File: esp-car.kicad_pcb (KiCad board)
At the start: 2 copper layers, 29 parts, among them J1 Conn_01x07_Socket, J2 Conn_01x07_Socket, U1 ESP32-DEVKIT-V1, U3 L293D

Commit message: esp_car 3.1
30/09 1:06
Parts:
- added ALI1: Conn_01x02_Socket, Connector_PinSocket_2.54mm:PinSocket_1x02_P2.54mm_Vertical, F.Cu at (180.9, 173.1)
- added INF_C1: Conn_01x06_Socket, Connector_PinSocket_2.54mm:PinSocket_1x06_P2.54mm_Vertical, F.Cu at (150.6, 53.0)
- added INF_FD1: Conn_01x06_Socket, Connector_PinSocket_2.54mm:PinSocket_1x06_P2.54mm_Vertical, F.Cu at (180.6, 49.4)
- added INF_FE1: Conn_01x06_Socket, Connector_PinSocket_2.54mm:PinSocket_1x06_P2.54mm_Vertical, F.Cu at (132.6, 49.4)
- added INF_TE1: Conn_01x06_Socket, Connector_PinSocket_2.54mm:PinSocket_1x06_P2.54mm_Vertical, F.Cu at (194.7, 155.8)
- added MotorD1: Conn_01x02_Socket, Connector_PinSocket_2.54mm:PinSocket_1x02_P2.54mm_Vertical, F.Cu at (185.5, 173.1)
- added MotorE1: Conn_01x02_Socket, Connector_PinSocket_2.54mm:PinSocket_1x02_P2.54mm_Vertical, F.Cu at (190.1, 173.1)
- J1, J2: moved to B.Cu
- moved EN2 87.1 mm to (178.2, 146.5)
- moved BotaoRotatorio1 76.2 mm to (138.0, 142.0)
- moved LED1 76.2 mm to (134.5, 194.1)
- moved R10 76.2 mm to (161.2, 158.0)
- moved Re2 76.2 mm to (166.2, 185.0)
- moved TelaOLED1 76.2 mm to (138.0, 156.5)
- moved BZ1 76.2 mm to (150.5, 168.8)
- moved C1 76.2 mm to (150.5, 183.5)
- moved EN1 76.2 mm to (143.0, 159.0)
- moved R220 76.2 mm to (161.2, 184.8)
- moved R9 76.2 mm to (161.2, 177.7)
- moved Re1 76.2 mm to (155.2, 154.5)
- moved U3 76.2 mm to (133.4, 168.9)
- moved giroscopio1 76.2 mm to (133.5, 148.9)
- moved R2 69.5 mm to (118.7, 46.8), turned to 180 degrees
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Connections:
- BotaoRotatorio1 pad 5: 5V -> 3.3V
- C1 pad 1: 5V -> GND
- C1 pad 2: 5VI -> VIN
- EN1 pad 1: Net-(EN1-Pin_1) -> OUTE
- EN1 pad 3: 5V -> 3.3V
- EN2 pad 1: Net-(EN2-Pin_1) -> OUTD
- EN2 pad 3: 5V -> 3.3V
- J1 pad 4: 5V -> 3.3V
- J2 pad 4: 5V -> 3.3V
- R1 pad 1: 5V -> 3.3V
- R2 pad 2: 5V -> 3.3V
- R3 pad 2: 5V -> 3.3V
- R4 pad 1: 5V -> 3.3V
- R5 pad 1: 5V -> 3.3V
- R6 pad 2: 5V -> 3.3V
- R7 pad 1: 5V -> 3.3V
- R8 pad 2: 5V -> 3.3V
- TelaOLED1 pad 4: 5V -> 3.3V
- U1 pad 1: unconnected-(U1-3V3-Pad1) -> 3.3V
- U1 pad 12: CD -> unconnected-(U1-RX0-Pad12)
- U1 pad 13: INF_C -> unconnected-(U1-TX0-Pad13)
- U1 pad 21: unconnected-(U1-D32-Pad21) -> CD
- U1 pad 30: 5V -> VIN
- U3 pad 1: 5V -> 3.3V
- U3 pad 16: 5V -> VIN
- U3 pad 9: 5V -> 3.3V
- giroscopio1 pad 7: 5V -> 3.3V

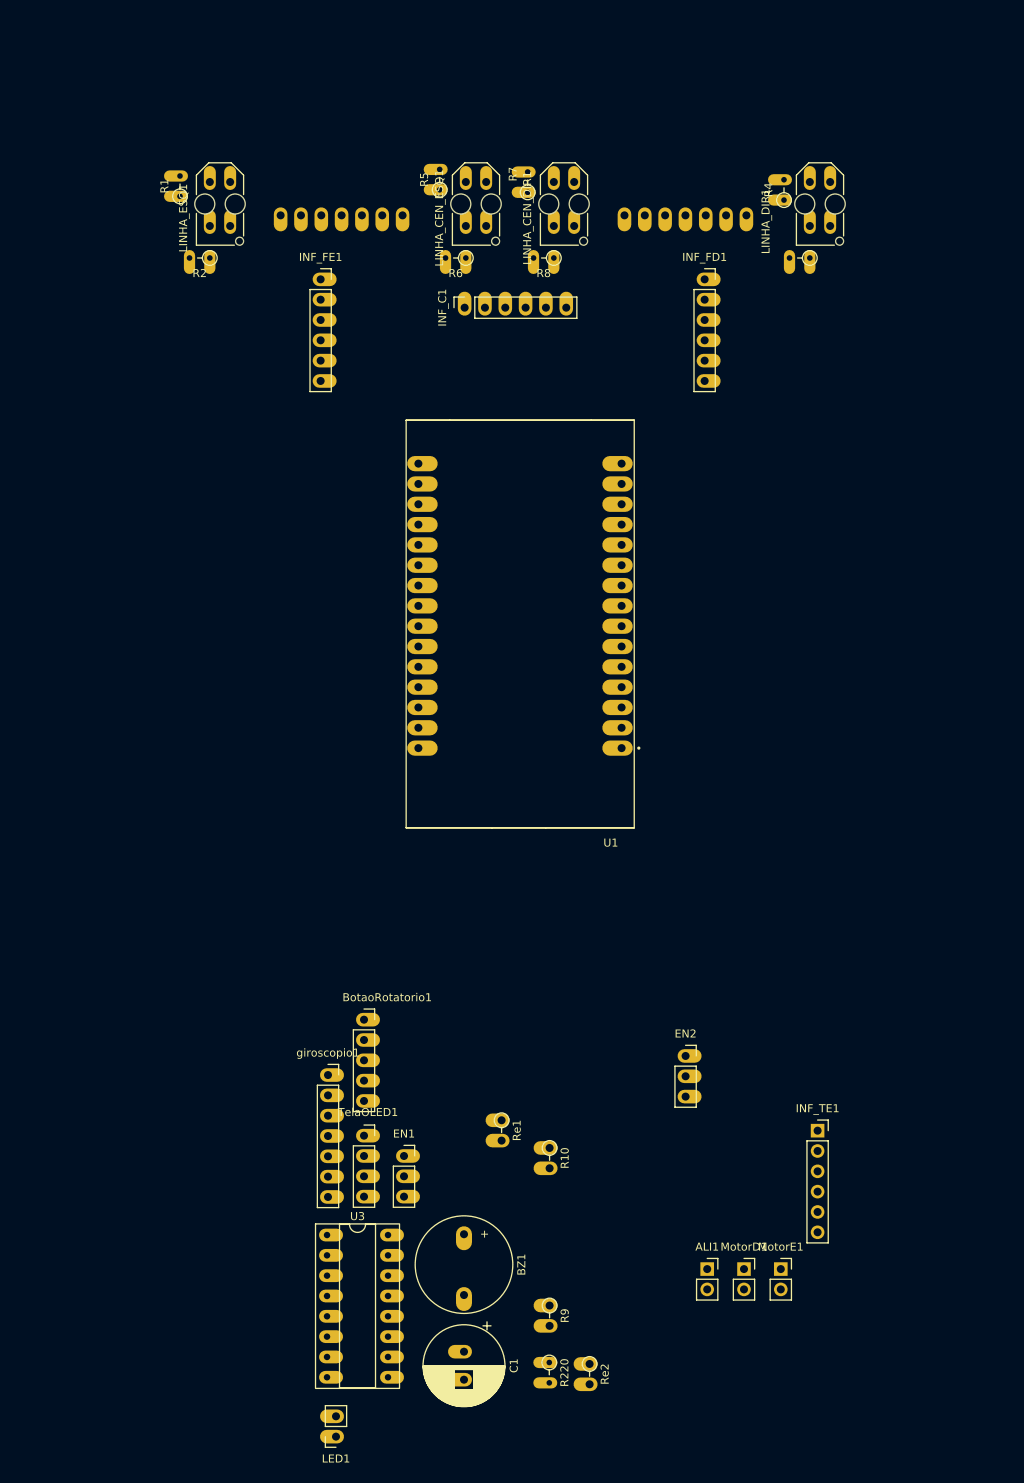
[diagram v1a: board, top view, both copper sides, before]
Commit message: esp-car 3.2
trilhas de cimas feitas, precisa arrumar resistores
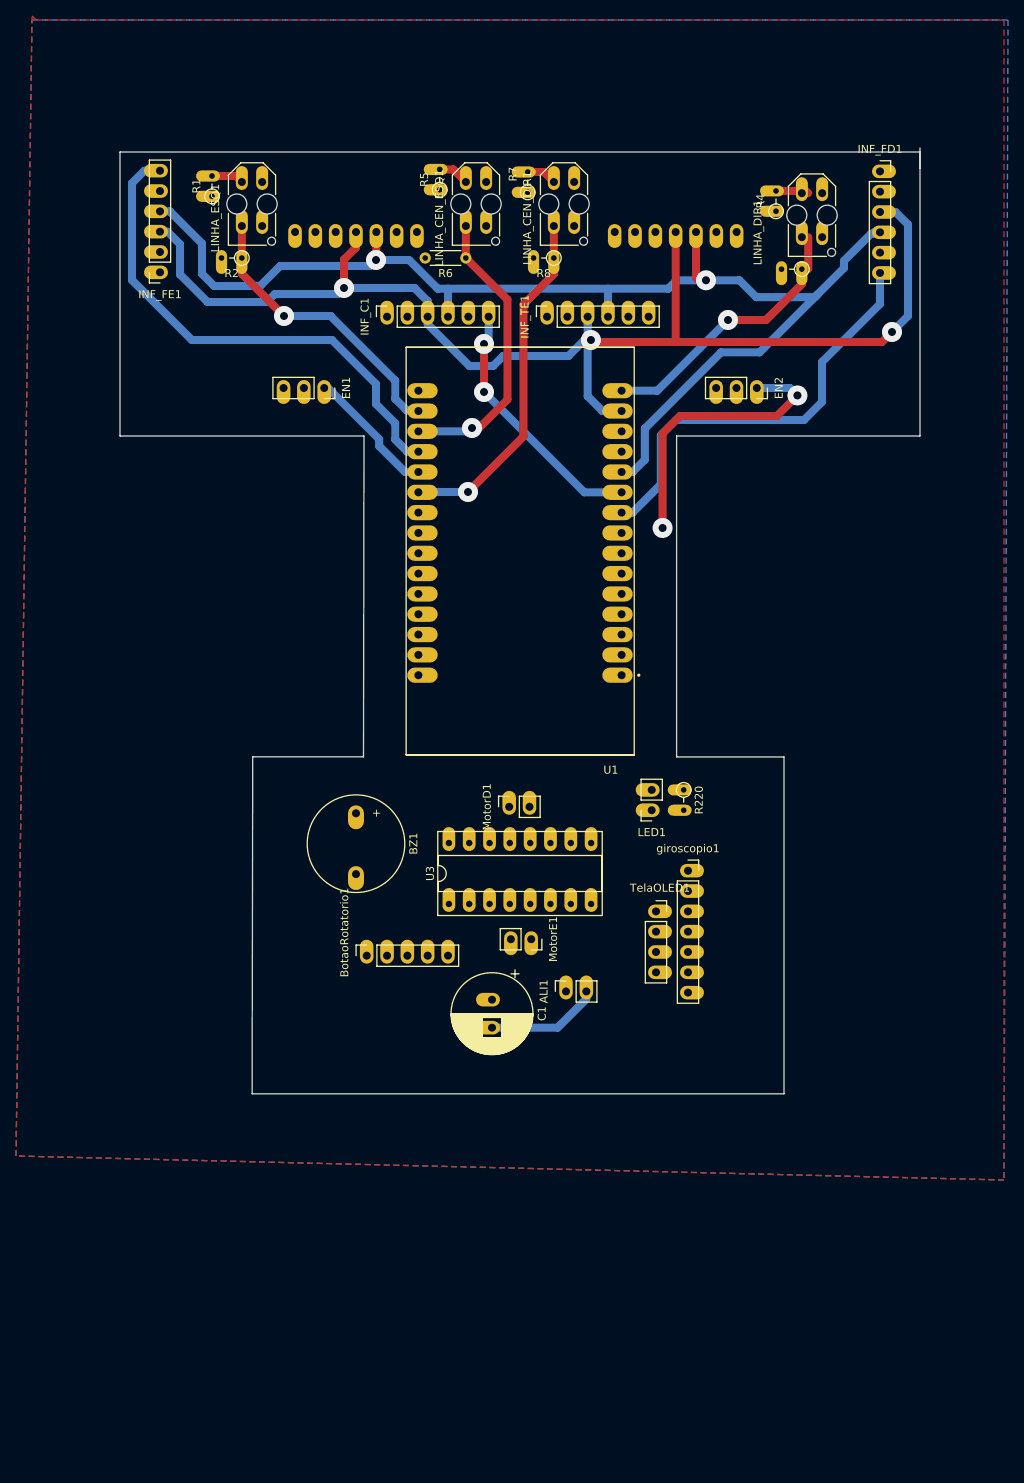
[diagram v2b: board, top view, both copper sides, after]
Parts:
- removed R10, R9: 1K, Resistor_THT:R_Axial_DIN0204_L3.6mm_D1.6mm_P2.54mm_Vertical
- removed Re1, Re2: 2K, Resistor_THT:R_Axial_DIN0204_L3.6mm_D1.6mm_P2.54mm_Vertical
- R6: footprint Resistor_THT:R_Axial_DIN0204_L3.6mm_D1.6mm_P2.54mm_Vertical -> Resistor_THT:R_Axial_DIN0204_L3.6mm_D1.6mm_P5.08mm_Horizontal
- moved INF_TE1 107.2 mm to (160.9, 54.1), turned to 90 degrees
- moved EN1 96.5 mm to (133.0, 63.0), turned to -90 degrees
- moved LED1 87.7 mm to (174.0, 115.8)
- moved EN2 84.0 mm to (187.1, 63.0), turned to -90 degrees
- moved R220 73.5 mm to (178.0, 113.2)
- moved MotorD1 64.8 mm to (156.2, 115.4), turned to 90 degrees
- moved BZ1 54.3 mm to (137.0, 116.2)
- moved giroscopio1 51.7 mm to (178.5, 123.3)
- moved MotorE1 51.7 mm to (158.9, 131.9), turned to -90 degrees
- moved TelaOLED1 46.0 mm to (174.5, 128.4)
- moved C1 44.1 mm to (154.0, 139.5)
- moved U3 44.1 mm to (148.6, 127.5), turned to 90 degrees
- moved ALI1 38.9 mm to (163.2, 138.4), turned to 90 degrees
- moved INF_FD1 25.7 mm to (202.5, 35.9)
- moved INF_FE1 20.1 mm to (112.5, 48.5), turned to 180 degrees
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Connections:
- J1 pad 2: SDA -> GND
- J1 pad 3: SCL -> 3.3V
- J1 pad 4: 3.3V -> SCL
- J1 pad 5: GND -> SDA
- J2 pad 2: SDA -> GND
- J2 pad 3: SCL -> 3.3V
- J2 pad 4: 3.3V -> SCL
- J2 pad 5: GND -> SDA
- U1 pad 15: OUTD -> LD
- U1 pad 19: INF_FE -> INF_TE
- U1 pad 20: unconnected-(U1-D35-Pad20) -> OUTE
- U1 pad 22: OUTE -> unconnected-(U1-D33-Pad22)
- U1 pad 25: INF_TE -> unconnected-(U1-D27-Pad25)
- U1 pad 9: LD -> INF_D
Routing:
- net SCL: track 0.00 -> 160.9 mm, vias 0 -> 3
- net SDA: track 0.00 -> 157.7 mm, vias 0 -> 2
- net INF_TE: track 0.00 -> 63.6 mm
- net INF_D: track 0.00 -> 53.5 mm
- net CD: track 0.00 -> 43.9 mm, vias 0 -> 1
- net LE: track 0.00 -> 37.3 mm, vias 0 -> 1
- net CE: track 0.00 -> 36.6 mm, vias 0 -> 1
- net OUTD: track 0.00 -> 36.1 mm, vias 0 -> 2
- net LD: track 0.00 -> 33.9 mm, vias 0 -> 1
- net INF_FD: track 0.00 -> 32.0 mm, vias 0 -> 2
- net OUTE: track 0.00 -> 16.6 mm
- net VIN: track 0.00 -> 14.2 mm
- net Net-(LINHA_ESQ1-PadA): track 0.00 -> 4.04 mm
- net Net-(LINHA_CEN_ESQ1-PadA): track 0.00 -> 3.92 mm
- net Net-(LINHA_CEN_DIR1-PadA): track 0.00 -> 3.79 mm
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- added copper zone on F.Cu, net 3.3V
- added copper zone on B.Cu, net GND
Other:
- board outline added: 100 x 118.2 mm

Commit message: esp-car 3.3
furação mais metade da parte de baixo completa
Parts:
- added H1: MountingHole, MountingHole:MountingHole_3.2mm_M3, F.Cu at (201.5, 63.5)
- added H2: MountingHole, MountingHole:MountingHole_3.2mm_M3, F.Cu at (113.5, 63.5)
- added H3: MountingHole, MountingHole:MountingHole_3.2mm_M3, F.Cu at (184.5, 146.2)
- added H4: MountingHole, MountingHole:MountingHole_3.2mm_M3, F.Cu at (130.0, 146.2)
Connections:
- U1 pad 24: IN1 -> S1
- U1 pad 25: unconnected-(U1-D27-Pad25) -> S2
- U1 pad 26: KEY -> BUZZ
- U1 pad 27: LED -> KEY
- U1 pad 28: BUZZ -> IN1
- U1 pad 3: S1 -> unconnected-(U1-D15-Pad3)
- U1 pad 5: S2 -> unconnected-(U1-D4-Pad5)
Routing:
- net IN1: track 0.00 -> 69.5 mm
- net VIN: track 14.2 -> 83.4 mm, vias 0 -> 3
- net S1: track 0.00 -> 59.2 mm
- net S2: track 0.00 -> 55.9 mm
- net KEY: track 0.00 -> 52.5 mm
- net IN4: track 0.00 -> 46.3 mm
- net BUZZ: track 0.00 -> 30.3 mm
- net OUT3: track 0.00 -> 5.62 mm
- net OUT4: track 0.00 -> 5.54 mm
- net OUT1: track 0.00 -> 5.51 mm
- net OUT2: track 0.00 -> 5.40 mm
- net SDA: track 157.7 -> 161.7 mm
- net SCL: track 160.9 -> 164.9 mm
- net Net-(LED1-Pin_2): track 0.00 -> 4.00 mm
